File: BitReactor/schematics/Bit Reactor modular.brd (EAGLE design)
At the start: 100 x 50 mm, 113 parts, among them IC1 TL074D, U1 ADC0808N, U2 4053D, U3 4053D, U4 741G3157DBVR, U5 TL072D, U6 LM3914N, U7 LM555D

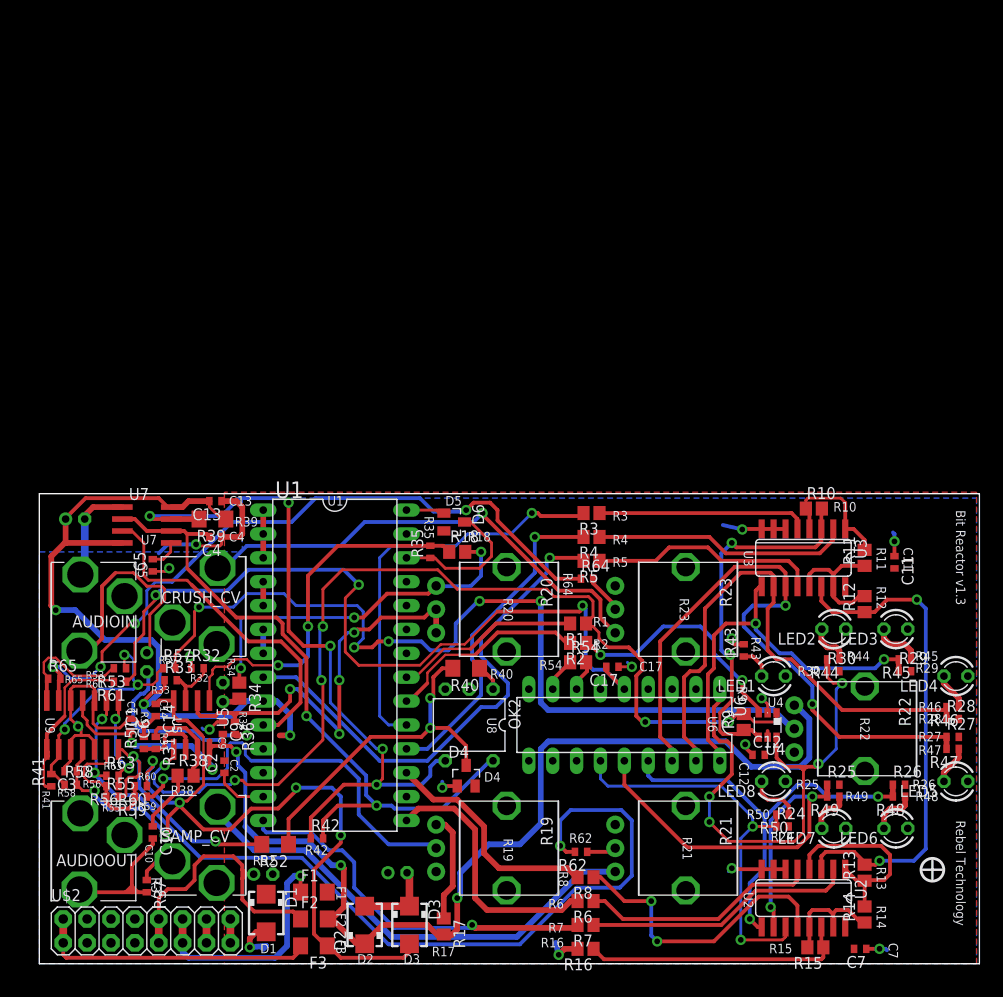
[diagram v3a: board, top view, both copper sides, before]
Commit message: turned board upright
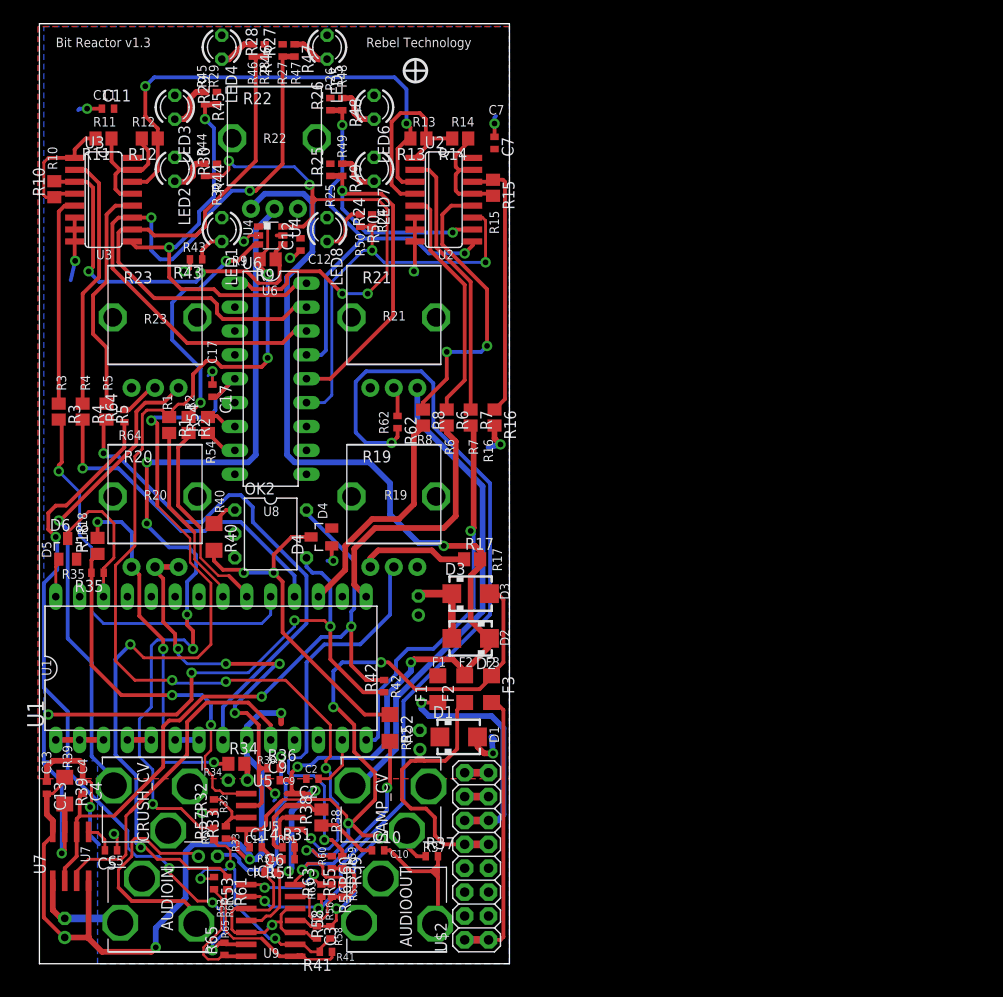
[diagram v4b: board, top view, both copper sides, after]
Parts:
- moved LED5 102.8 mm to (30.6, 97.5), turned to 270 degrees
- moved LED4 102.8 mm to (19.4, 97.5), turned to 270 degrees
- moved R46 102.1 mm to (22.7, 97.2), turned to 270 degrees
- moved R47 102.1 mm to (27.1, 97.2), turned to 270 degrees
- moved R28 102.0 mm to (24.0, 97.2), turned to 90 degrees
- moved R27 102.0 mm to (25.9, 97.2), turned to 90 degrees
- moved C11 96.6 mm to (7.30, 91.0), turned to 0 degrees
- moved R45 95.4 mm to (17.6, 92.1), turned to 270 degrees
- moved R29 95.2 mm to (18.9, 92.1), turned to 90 degrees
- moved LED6 94.7 mm to (35.6, 91.1), turned to 270 degrees
- moved LED3 94.7 mm to (14.4, 91.1), turned to 270 degrees
- moved R48 94.5 mm to (32.2, 91.4), turned to 270 degrees
- moved R26 94.3 mm to (31.0, 91.4), turned to 90 degrees
- moved C7 94.1 mm to (48.4, 87.3), turned to 270 degrees
- moved R14 93.1 mm to (44.8, 87.8), turned to 180 degrees
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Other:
- board size 100 x 50 mm -> 50 x 100 mm
